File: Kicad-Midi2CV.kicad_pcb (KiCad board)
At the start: 2 copper layers, 99.7 x 99.7 mm, 67 parts, among them IC1 MCP4725module, IC2 MCP4725module, J1 Vin 7-12v, J10 Gate1, J11 Gate2, J12 Gate3, J13 Gate4, J2 MIDI OUT, J3 CV in, J4 Conn_01x04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

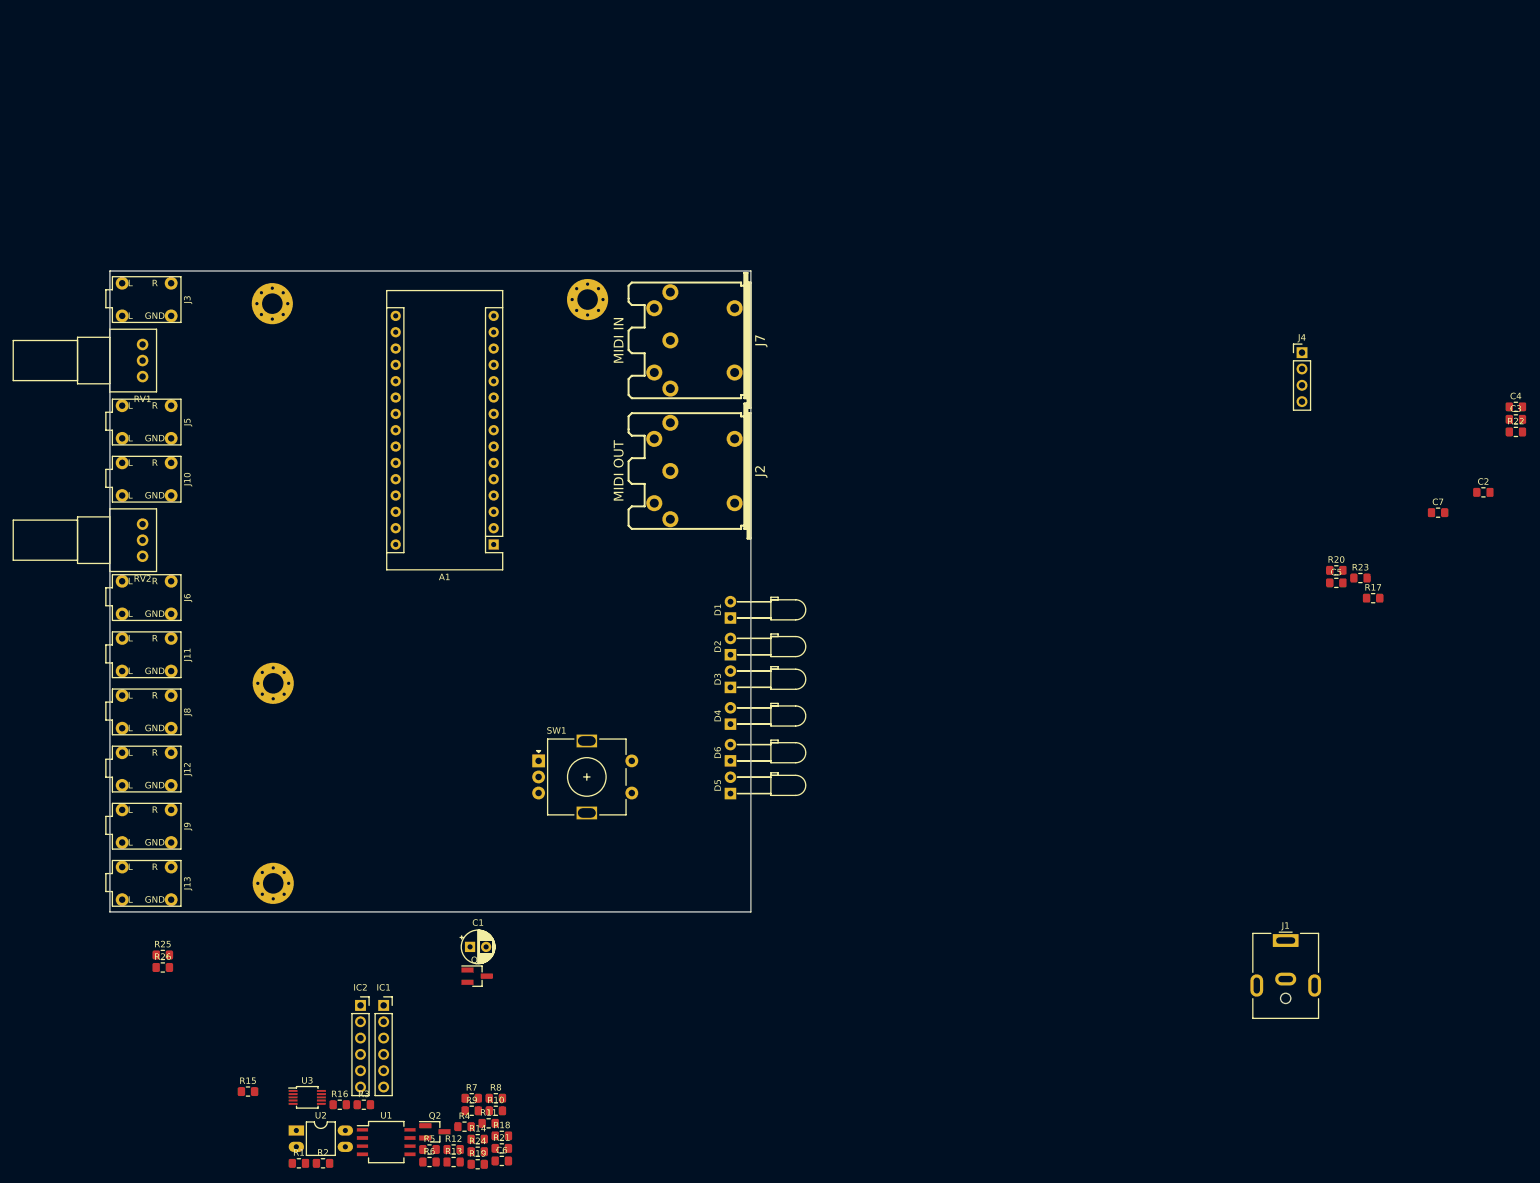
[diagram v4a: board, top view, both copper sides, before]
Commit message: Fixed Analog voltage
Encoder module replace
PCB reorganize
Added Analogue supply - not done
changed Jacks
etc
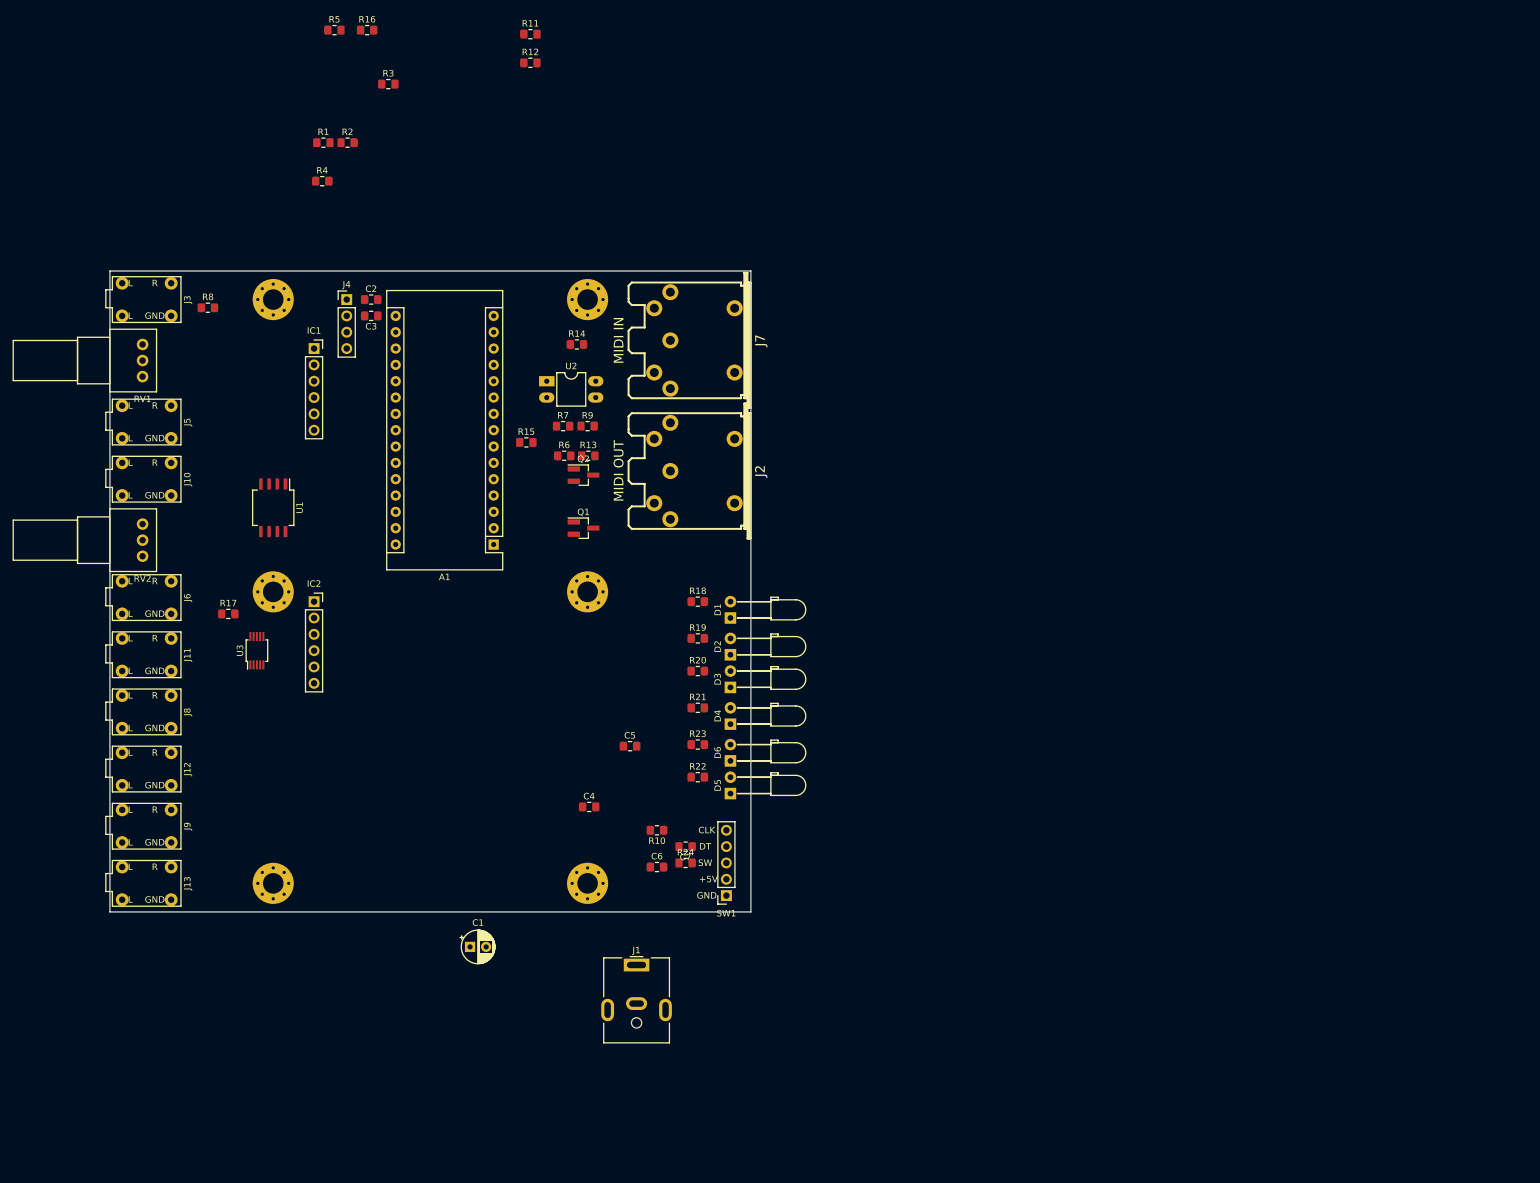
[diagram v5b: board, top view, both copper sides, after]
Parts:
- removed NA (x4): Mounting3.2mm, MountingHole:MountingHole_3.2mm_M3_Pad_Via
- removed R25, R26: 10k, Resistor_SMD:R_0805_2012Metric_Pad1.15x1.40mm_HandSolder
- added REF**: Mounting_3.2mm, MountingHole:MountingHole_3.2mm_M3_Pad_Via, F.Cu at (99.7, 120.7)
- added REF**: Mounting_3.2mm, MountingHole:MountingHole_3.2mm_M3_Pad_Via, F.Cu at (99.7, 29.8)
- added REF**: Mounting_3.2mm, MountingHole:MountingHole_3.2mm_M3_Pad_Via, F.Cu at (99.7, 75.3)
- added REF**: Mounting_3.2mm, MountingHole:MountingHole_3.2mm_M3_Pad_Via, F.Cu at (50.8, 120.7)
- added REF**: Mounting_3.2mm, MountingHole:MountingHole_3.2mm_M3_Pad_Via, F.Cu at (50.8, 75.3)
- added REF**: Mounting_3.2mm, MountingHole:MountingHole_3.2mm_M3_Pad_Via, F.Cu at (50.8, 29.8)
- C2: value C -> 100n
- SW1: value Encoder_Selector -> KY40_Rotary_Encoder_Module; footprint Rotary_Encoder:RotaryEncoder_Alps_EC11E-Switch_Vertical_H20mm -> Rotary_Encoder:KY-40-rotary-encoder-board
- moved C3 178.8 mm to (66.0, 32.4), turned to 180 degrees
- moved R17 178.1 mm to (43.8, 78.7)
- moved C2 175.6 mm to (66.0, 29.8)
- moved R5 174.7 mm to (60.3, -12.1)
- moved R11 169.5 mm to (90.8, -11.4)
- moved R12 169.4 mm to (90.8, -6.99)
- moved R16 167.2 mm to (65.4, -12.1)
- moved R1 158.8 mm to (58.6, 5.44)
- moved R2 158.8 mm to (62.4, 5.44)
- moved R3 158.8 mm to (68.7, -3.67)
- moved C4 157.0 mm to (99.9, 108.8)
- moved J4 148.8 mm to (62.2, 29.8)
- moved R4 148.7 mm to (58.4, 11.4)
- moved R22 138.1 mm to (116.8, 104.1)
- moved R8 130.9 mm to (40.6, 31.1)
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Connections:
- C6 pad 1: Net-(C6-Pad1) -> A1
- C7 pad 1: Net-(C7-Pad1) -> A2
- R24 pad 1: Net-(R24-Pad1) -> Btn
- R24 pad 2: Btn -> Net-(R24-Pad2)

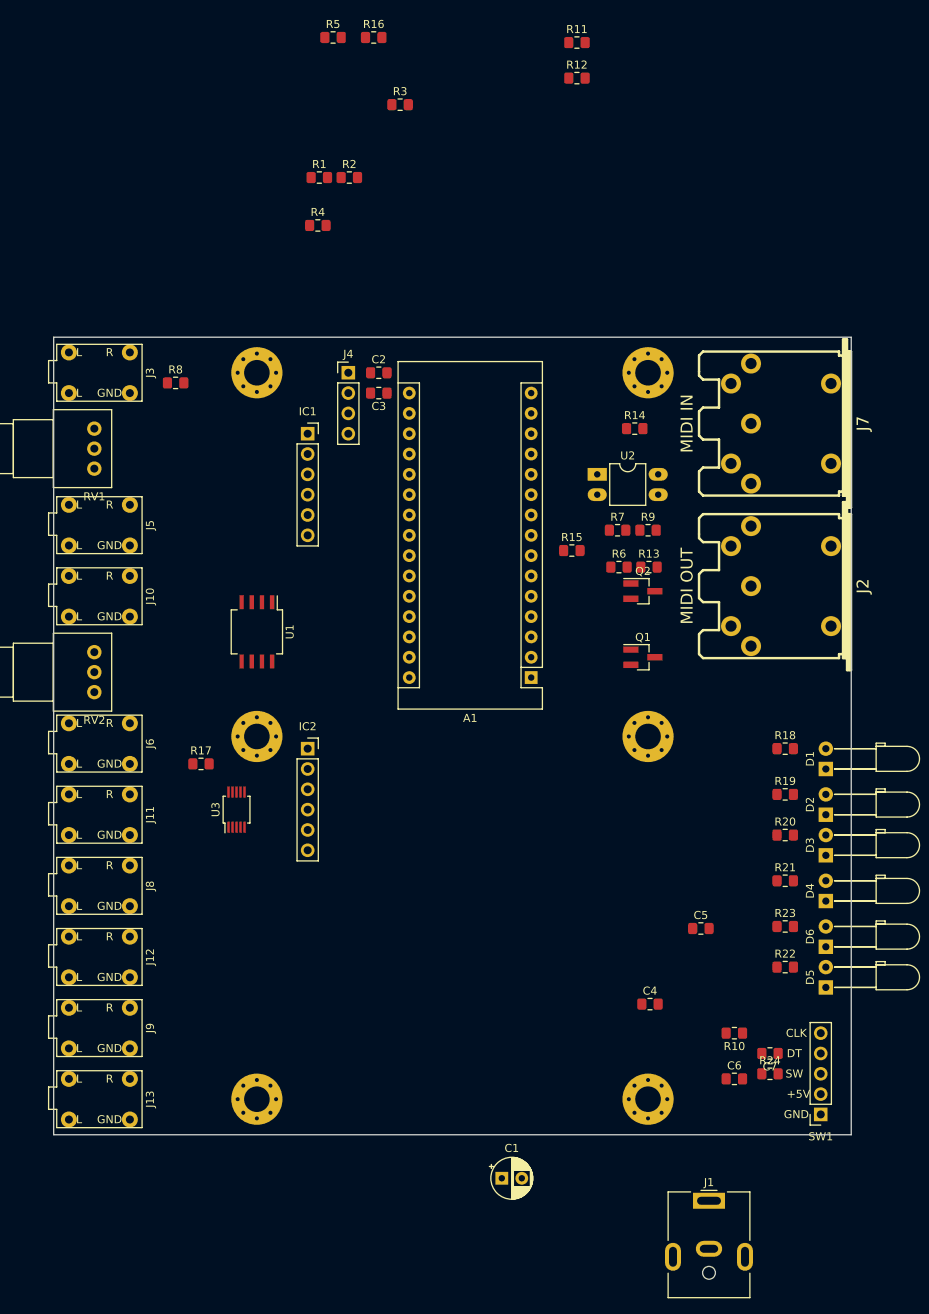
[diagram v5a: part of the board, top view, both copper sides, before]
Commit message: organizing PCB placement
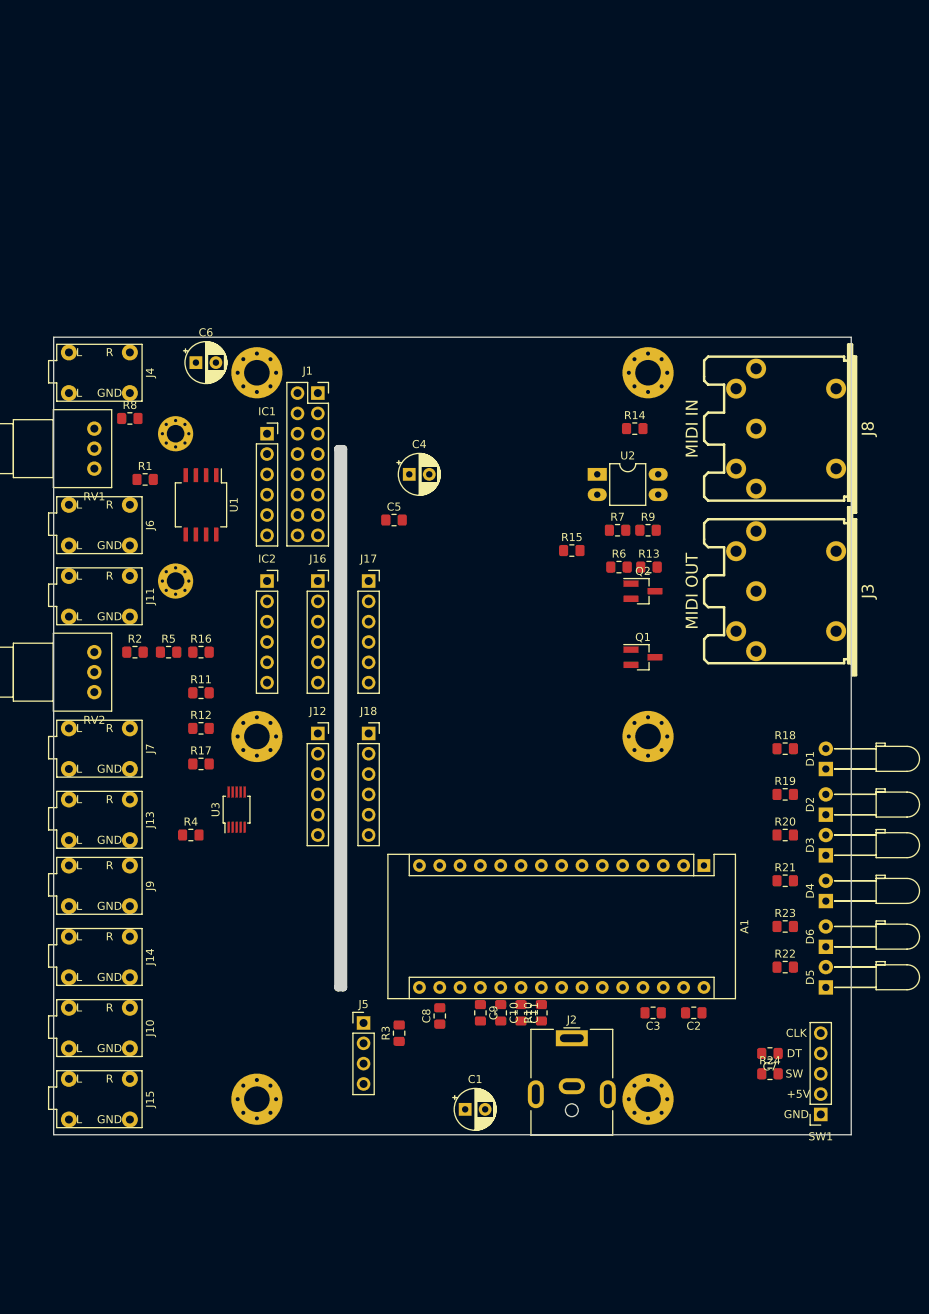
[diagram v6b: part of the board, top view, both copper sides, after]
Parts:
- added C10: 10n, Capacitor_SMD:C_0805_2012Metric_Pad1.15x1.40mm_HandSolder, F.Cu at (81.3, 109.9)
- added C11: 10n, Capacitor_SMD:C_0805_2012Metric_Pad1.15x1.40mm_HandSolder, F.Cu at (83.8, 109.9)
- added C8: C, Capacitor_SMD:C_0805_2012Metric_Pad1.15x1.40mm_HandSolder, F.Cu at (73.7, 110.2)
- added C9: 10n, Capacitor_SMD:C_0805_2012Metric_Pad1.15x1.40mm_HandSolder, F.Cu at (78.7, 109.9)
- added J14: Gate3, Connector_Audio:AudioJack3StereoNarrow-PJ-321, F.Cu at (31.1, 102.9)
- added J15: Gate4, Connector_Audio:AudioJack3StereoNarrow-PJ-321, F.Cu at (31.1, 120.7)
- added J16: I2C_Conn, Connector_PinSocket_2.54mm:PinSocket_1x06_P2.54mm_Vertical, F.Cu at (58.4, 55.9)
- added J17: I2C_Conn, Connector_PinSocket_2.54mm:PinSocket_1x06_P2.54mm_Vertical, F.Cu at (64.8, 55.9)
- added J18: GateConn, Connector_PinSocket_2.54mm:PinSocket_1x06_P2.54mm_Vertical, F.Cu at (64.8, 74.9)
- added REF**: M2_MCP4725, MountingHole:MountingHole_2.2mm_M2_Pad_Via, F.Cu at (40.6, 37.5)
- added REF**: M2_MCP4725, MountingHole:MountingHole_2.2mm_M2_Pad_Via, F.Cu at (40.6, 55.9)
- C1: value CP -> 100uF
- C3: value C -> 100n
- C4: value C -> 100uF 16v; footprint Capacitor_SMD:C_0805_2012Metric_Pad1.15x1.40mm_HandSolder -> Capacitor_THT:CP_Radial_D5.0mm_P2.50mm
- C5, C7: value 10n -> 100n
- C6: value 10n -> 100uF 16v; footprint Capacitor_SMD:C_0805_2012Metric_Pad1.15x1.40mm_HandSolder -> Capacitor_THT:CP_Radial_D5.0mm_P2.50mm
- J1: value Vin 7-12v -> Doepfer connector; footprint Connector_BarrelJack:BarrelJack_CUI_PJ-063AH_Horizontal -> Connector_PinSocket_2.54mm:PinSocket_2x08_P2.54mm_Vertical
- J10: value Gate1 -> CV4
- J11: value Gate2 -> Gate1
- J12: value Gate3 -> GateConn; footprint Connector_Audio:AudioJack3StereoNarrow-PJ-321 -> Connector_PinSocket_2.54mm:PinSocket_1x06_P2.54mm_Vertical
- J13: value Gate4 -> Gate2
- J2: value MIDI OUT -> Vin 7-12v; footprint w_conn_av:din-5 -> Connector_BarrelJack:BarrelJack_CUI_PJ-063AH_Horizontal
- J3: value CV in -> MIDI OUT; footprint Connector_Audio:AudioJack3StereoNarrow-PJ-321 -> w_conn_av:din-5
- J4: value Conn_01x04 -> CV in; footprint Connector_PinHeader_2.54mm:PinHeader_1x04_P2.54mm_Vertical -> Connector_Audio:AudioJack3StereoNarrow-PJ-321
- J5: value CV1 -> Power Conn; footprint Connector_Audio:AudioJack3StereoNarrow-PJ-321 -> Connector_PinHeader_2.54mm:PinHeader_1x04_P2.54mm_Vertical
- J6: value CV2 -> CV1
- J7: value MIDI IN -> CV2; footprint w_conn_av:din-5 -> Connector_Audio:AudioJack3StereoNarrow-PJ-321
- J8: value CV3 -> MIDI IN; footprint Connector_Audio:AudioJack3StereoNarrow-PJ-321 -> w_conn_av:din-5
- J9: value CV4 -> CV3
- moved R3 116.1 mm to (68.6, 112.4), turned to 90 degrees
- moved J1 112.2 mm to (58.4, 32.4)
- moved C6 112.0 mm to (43.2, 28.6)
- moved J8 102.5 mm to (116.2, 36.8), turned to 90 degrees
- moved R11 93.9 mm to (43.8, 69.8)
- moved R12 93.9 mm to (43.8, 74.3)
- moved J7 93.7 mm to (31.1, 76.8), turned to 0 degrees
- moved J3 89.4 mm to (116.2, 57.1), turned to 90 degrees
- moved C2 89.2 mm to (105.4, 109.9), turned to 180 degrees
- moved C3 84.7 mm to (100.3, 109.9)
- moved R16 79.8 mm to (43.8, 64.8)
- moved R5 79.5 mm to (39.8, 64.8)
- moved R4 77.8 mm to (42.5, 87.6)
- moved C4 72.7 mm to (69.8, 42.5)
- moved J5 70.4 mm to (64.1, 111.1)
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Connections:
- A1 pad 25: (no net) -> A6
- A1 pad 26: (no net) -> A7
- C4 pad 1: GND -> /12v
- C4 pad 2: Net-(A1-Pad17) -> GND
- C5 pad 1: Btn -> GND
- C5 pad 2: GND -> /12v
- C6 pad 1: A1 -> GND
- C6 pad 2: GND -> /-12v
- C7 pad 1: A2 -> /-12v
- J1 pad 1: VCC -> Net-(J1-Pad1)
- J1 pad 2: GND -> Net-(J1-Pad1)
- J10 pad T: Gate1 -> CV4
- J11 pad T: Gate2 -> Gate1
- J13 pad T: Gate4 -> Gate2
- J2 pad 1: (no net) -> VCC
- J2 pad 2: (no net) -> GND
- J6 pad T: CV2Gain -> CV1Gain
- J9 pad T: CV4 -> CV3
- R14 pad 2: Net-(J7-Pad4) -> Net-(J8-Pad4)
- R7 pad 2: Net-(J2-Pad4) -> Net-(J3-Pad4)
- R8 pad 1: Net-(J3-PadT) -> Net-(J4-PadT)
- U1 pad 4: (no net) -> /-12v
- U1 pad 8: (no net) -> /12v
- U2 pad 2: Net-(J7-Pad5) -> Net-(J8-Pad5)
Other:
- outline, holes or cut-outs redrawn
